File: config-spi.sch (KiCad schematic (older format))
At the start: 43 parts, among them J1 0878311420, J8 61300411121, Q7 BSS138APW, Q8 BSS138APW, U1 XC7K70T-FBG484, U3 S25FL128SAGNFI000

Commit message: Remove XADC circuit
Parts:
- removed C11: C_10n_0402, lpddr4-test-board-footprints:0402-cap, symbol lpddr4-test-board:C_10n_0402
- removed C9: C_1n_0402, lpddr4-test-board-footprints:0402-res, symbol lpddr4-test-board:C_1n_0402
- removed J8: 61300411121, lpddr4-test-board-footprints:PinHeader_1x4_P2.54mm_Drill1.02mm, symbol lpddr4-test-board:61300411121
- removed R18, R19: R_140R_0402, lpddr4-test-board-footprints:0402-res, symbol lpddr4-test-board:R_140R_0402
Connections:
- net labels removed: V_N, V_P, XADCGND, XADCVREF, XADC_V_N, XADC_V_P
- wire segments 158 -> 152
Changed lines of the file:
@@
 $EndDescr
 Wire Wire Line
-	11675 6100 10950 6100
-Text GLabel 10950 6100 0    50   Input ~ 0
-V_P
-Wire Wire Line
-	11675 6200 10950 6200
-Text GLabel 10950 6200 0    50   Input ~ 0
-V_N
+	11675 6100 11100 6100
+Wire Wire Line
+	11675 6200 11100 6200
 Wire Wire Line
 	11675 4700 10950 4700
@@
 Text GLabel 8375 9475 0    50   Input ~ 0
 MODE1
-Wire Wire Line
-	13475 8950 13800 8950
-Wire Wire Line
-	13475 9250 13825 9250
-Text GLabel 13475 8950 0    50   Input ~ 0
-XADC_V_P
-Text GLabel 13475 9250 0    50   Input ~ 0
-XADC_V_N
-Text GLabel 14925 8950 2    50   Input ~ 0
-V_P
-Text GLabel 14925 9250 2    50   Input ~ 0
-V_N
-$Comp
-L lpddr4-test-board:R_140R_0402 R18
-U 1 1 611C8786
-P 13950 8950
-F 0 "R18" H 13900 9050 60  0000 C CNN
-F 1 "R_140R_0402" H 13950 8800 60  0001 C CNN
-F 2 "lpddr4-test-board-footprints:0402-res" H 14150 9150 60  0001 L CNN
-F 3 "" H 13950 8950 50  0001 C CNN
-F 4 "MULTICOMP PRO" H 14150 9350 60  0001 L CNN "Manufacturer"
-F 5 "MCMR04X1400FTL" H 14150 9250 60  0001 L CNN "MPN"
-F 6 "140R" H 14150 8900 50  0000 C CNN "Val"
-	1    13950 8950
-	1    0    0    -1
-$EndComp
-$Comp
-L lpddr4-test-board:R_140R_0402 R19
-U 1 1 611C9205
-P 13975 9250
-F 0 "R19" H 13925 9350 60  0000 C CNN
-F 1 "R_140R_0402" H 13975 9100 60  0001 C CNN
-F 2 "lpddr4-test-board-footprints:0402-res" H 14175 9450 60  0001 L CNN
-F 3 "" H 13975 9250 50  0001 C CNN
-F 4 "MULTICOMP PRO" H 14175 9650 60  0001 L CNN "Manufacturer"
-F 5 "MCMR04X1400FTL" H 14175 9550 60  0001 L CNN "MPN"
-F 6 "140R" H 14175 9200 50  0000 C CNN "Val"
-	1    13975 9250
-	1    0    0    -1
-$EndComp
-$Comp
-L lpddr4-test-board:C_1n_0402 C9
-U 1 1 61217549
-P 14400 9100
-F 0 "C9" H 14425 9200 60  0000 L CNN
-F 1 "C_1n_0402" H 14400 8950 60  0001 C CNN
-F 2 "lpddr4-test-board-footprints:0402-res" H 14600 9300 60  0001 L CNN
-F 3 "" H 14400 9100 50  0001 C CNN
-F 4 "YAGEO" H 14600 9500 60  0001 L CNN "Manufacturer"
-F 5 "CC0402KRX7R9BB102" H 14600 9400 60  0001 L CNN "MPN"
-F 6 "1n" H 14425 9000 50  0000 L CNN "Val"
-	1    14400 9100
-	1    0    0    -1
-$EndComp
-Wire Wire Line
-	14100 8950 14400 8950
-Wire Wire Line
-	14125 9250 14400 9250
-Connection ~ 14400 8950
-Connection ~ 14400 9250
-Wire Wire Line
-	14400 8950 14925 8950
-Wire Wire Line
-	14400 9250 14925 9250
 Text Notes 1225 8500 0    118  ~ 24
 JTAG Connector\n
@@
 Text GLabel 8750 5600 0    50   Input ~ 0
 INIT_B
-Text GLabel 10950 6500 0    50   Input ~ 0
-XADCGND
-Wire Wire Line
-	11675 6500 10950 6500
-Text GLabel 10950 6400 0    50   Input ~ 0
-XADCVREF
-Wire Wire Line
-	11675 6400 10950 6400
-Wire Wire Line
-	11675 6700 11550 6700
-Wire Wire Line
-	11550 6700 11550 6800
-Wire Wire Line
-	11675 6800 11550 6800
-Connection ~ 11550 6800
-Wire Wire Line
-	11550 6800 11550 7025
+Wire Wire Line
+	11675 6500 11100 6500
+Wire Wire Line
+	11675 6700 11100 6700
+Wire Wire Line
+	11100 6700 11100 6800
+Wire Wire Line
+	11675 6800 11100 6800
+Connection ~ 11100 6800
+Wire Wire Line
+	11100 6800 11100 7000
 $Comp
 L lpddr4-test-board:GND #PWR0118
 U 1 1 61E5EC21
-P 11550 7025
-F 0 "#PWR0118" H 11550 6775 50  0001 C CNN
-F 1 "GND" H 11555 6852 50  0000 C CNN
-F 2 "" H 11550 7025 50  0001 C CNN
-F 3 "" H 11550 7025 50  0001 C CNN
-	1    11550 7025
-	1    0    0    -1
-$EndComp
-$Comp
-L lpddr4-test-board:C_10n_0402 C?
-U 1 1 61E688A4
-P 12575 9000
-AR Path="/600295C1/61E688A4" Ref="C?"  Part="1"
-AR Path="/5FD53C7D/61E688A4" Ref="C11"  Part="1"
-F 0 "C11" H 12600 9100 60  0000 L CNN
-F 1 "C_10n_0402" H 12575 8850 60  0001 C CNN
-F 2 "lpddr4-test-board-footprints:0402-cap" H 12775 9200 60  0001 L CNN
-F 3 "" H 12575 9000 50  0001 C CNN
-F 4 "AVX" H 12775 9400 60  0001 L CNN "Manufacturer"
-F 5 "04025G103ZAT2A" H 12775 9300 60  0001 L CNN "MPN"
-F 6 "10n" H 12600 8900 50  0000 L CNN "Val"
-	1    12575 9000
-	1    0    0    -1
-$EndComp
-Text GLabel 12575 9150 3    50   Input ~ 0
-XADCGND
+P 11100 7000
+F 0 "#PWR0118" H 11100 6750 50  0001 C CNN
+F 1 "GND" H 11105 6827 50  0000 C CNN
+F 2 "" H 11100 7000 50  0001 C CNN
+F 3 "" H 11100 7000 50  0001 C CNN
+	1    11100 7000
+	1    0    0    -1
+$EndComp
 Wire Wire Line
 	10150 5325 10150 5500
@@
 Wire Wire Line
 	10950 5000 11675 5000
-$Comp
-L lpddr4-test-board:61300411121 J8
-U 1 1 6AC614B6
-P 14350 7925
-F 0 "J8" V 14225 7900 50  0000 C CNN
-F 1 "61300411121" V 14775 7925 50  0000 C CNN
-F 2 "lpddr4-test-board-footprints:PinHeader_1x4_P2.54mm_Drill1.02mm" H 14550 8125 60  0001 L CNN
-F 3 "" H 14550 8225 60  0001 L CNN
-F 4 "61300411121" H 14550 8425 60  0001 L CNN "MPN"
-F 5 "Wurth Electronics Inc." H 14550 9025 60  0001 L CNN "Manufacturer"
-	1    14350 7925
-	0    1    1    0
-$EndComp
-Text GLabel 14875 7925 2    50   Input ~ 0
-XADC_V_P
-Text GLabel 14875 8025 2    50   Input ~ 0
-XADC_V_N
-Text GLabel 14875 8125 2    50   Input ~ 0
-XADCGND
-Text GLabel 14875 8225 2    50   Input ~ 0
-XADCVREF
-Wire Wire Line
-	14500 7925 14875 7925
-Wire Wire Line
-	14500 8025 14875 8025
-Wire Wire Line
-	14500 8125 14875 8125
-Wire Wire Line
-	14875 8225 14500 8225
 Text Notes 4550 8525 0    118  ~ 24
 STATUS LEDs
@@
 	0    -1   1    0
 $EndComp
-Text GLabel 12575 8850 1    50   Input ~ 0
-XADCVREF
 Text GLabel 9100 8975 2    50   Input ~ 0
 VCC3v3
@@
 	1    0    0    -1
 $EndComp
+Wire Wire Line
+	11100 6700 11100 6500
+Connection ~ 11100 6700
+Connection ~ 11100 6200
+Wire Wire Line
+	11100 6100 11100 6200
+Connection ~ 11100 6500
+Wire Wire Line
+	11100 6200 11100 6400
+Connection ~ 11100 6400
+Wire Wire Line
+	11100 6400 11100 6500
+Wire Wire Line
+	11100 6400 11675 6400
 $EndSCHEMATC

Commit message: Fix VCC labels
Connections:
- net labels removed: VCC3v3
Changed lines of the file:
@@
 	1    0    0    -1
 $EndComp
-Text GLabel 9800 4725 1    50   Input ~ 0
-VCC3v3
 $Comp
 L lpddr4-test-board:XC7K70T-FBG484 U1
@@
 Wire Wire Line
 	9475 4875 9800 4875
-Text GLabel 12075 3400 1    50   Input ~ 0
-VCC3v3
 Wire Wire Line
 	12075 3400 12075 3700
@@
 	12175 3700 12075 3700
 Connection ~ 12075 3700
-Text GLabel 14800 4300 1    50   Input ~ 0
-VCC3v3
 $Comp
 L lpddr4-test-board:C_47u_0603 C12
@@
 Wire Wire Line
 	5700 3525 5700 3250
-Text GLabel 5700 3150 1    50   Input ~ 0
-VCC3v3
 Wire Wire Line
 	5700 3825 5700 4550
@@
 	1625 9375 1625 9200
 Text GLabel 1625 9200 1    50   Input ~ 0
-VCC3v3
+VCC3V3
 Text GLabel 2575 9475 2    50   Input ~ 0
 TMS_JTAG
@@
 	8950 8975 9100 8975
 Text GLabel 9100 9475 2    50   Input ~ 0
-VCC3v3
+VCC3V3
 Wire Wire Line
 	8950 9475 9100 9475
@@
 	0    1    1    0
 $EndComp
-Text GLabel 11425 3400 1    50   Input ~ 0
-VCC3v3
 Wire Wire Line
 	11425 3400 11425 3775
@@
 	1    0    0    -1
 $EndComp
-Text GLabel 6175 5750 1    50   Input ~ 0
-VCC3v3
 Wire Wire Line
 	6175 5750 6175 5900
@@
 	0    -1   1    0
 $EndComp
-Text GLabel 9100 8975 2    50   Input ~ 0
-VCC3v3
 $Comp
 L antmicroRectangularConnectorsHeadersMalePins:62000311121 CFG1
@@
 	8550 10275 9125 10275
 Text GLabel 9125 9825 2    50   Input ~ 0
-VCC3v3
+VCC3V3
 $Comp
 L lpddr4-test-board:GND #PWR04
@@
 Wire Wire Line
 	11100 6400 11675 6400
+Text GLabel 9100 8975 2    50   Input ~ 0
+VCC3V3
+Text GLabel 12075 3400 1    50   Input ~ 0
+VCC3V3
+Text GLabel 11425 3400 1    50   Input ~ 0
+VCC3V3
+Text GLabel 14800 4300 1    50   Input ~ 0
+VCC3V3
+Text GLabel 9800 4725 1    50   Input ~ 0
+VCC3V3
+Text GLabel 6175 5750 1    50   Input ~ 0
+VCC3V3
+Text GLabel 5700 3150 1    50   Input ~ 0
+VCC3V3
 $EndSCHEMATC

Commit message: Replace VCC3V3 with 3V3_SYS
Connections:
- net labels added: 3V3_SYS
- net labels removed: VCC3V3
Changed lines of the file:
@@
 Connection ~ 14800 4750
 Text GLabel 2750 3950 1    50   Input ~ 0
-VCC3V3
+3V3_SYS
 Text GLabel 2425 3950 1    50   Input ~ 0
-VCC3V3
+3V3_SYS
 Wire Wire Line
 	2425 4250 2425 4300
@@
 	1625 9375 1625 9200
 Text GLabel 1625 9200 1    50   Input ~ 0
-VCC3V3
+3V3_SYS
 Text GLabel 2575 9475 2    50   Input ~ 0
 TMS_JTAG
@@
 	8950 8975 9100 8975
 Text GLabel 9100 9475 2    50   Input ~ 0
-VCC3V3
+3V3_SYS
 Wire Wire Line
 	8950 9475 9100 9475
@@
 	5325 9425 5350 9425
 Text GLabel 4925 9425 0    50   Input ~ 0
-VCC3V3
+3V3_SYS
 Wire Wire Line
 	4925 9425 5025 9425
@@
 	5350 10200 5375 10200
 Text GLabel 4950 10200 0    50   Input ~ 0
-VCC3V3
+3V3_SYS
 Wire Wire Line
 	4950 10200 5050 10200
@@
 	8550 10275 9125 10275
 Text GLabel 9125 9825 2    50   Input ~ 0
-VCC3V3
+3V3_SYS
 $Comp
 L lpddr4-test-board:GND #PWR04
@@
 	11100 6400 11675 6400
 Text GLabel 9100 8975 2    50   Input ~ 0
-VCC3V3
+3V3_SYS
 Text GLabel 12075 3400 1    50   Input ~ 0
-VCC3V3
+3V3_SYS
 Text GLabel 11425 3400 1    50   Input ~ 0
-VCC3V3
+3V3_SYS
 Text GLabel 14800 4300 1    50   Input ~ 0
-VCC3V3
+3V3_SYS
 Text GLabel 9800 4725 1    50   Input ~ 0
-VCC3V3
+3V3_SYS
 Text GLabel 6175 5750 1    50   Input ~ 0
-VCC3V3
+3V3_SYS
 Text GLabel 5700 3150 1    50   Input ~ 0
-VCC3V3
+3V3_SYS
 $EndSCHEMATC

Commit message: Update component library
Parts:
- CFG1: footprint antmicro-footprints:62000311121 -> lpddr4-test-board-footprints:62000311121; symbol antmicroRectangularConnectorsHeadersMalePins:62000311121 -> lpddr4-test-board:62000311121
- EMCCLK1, PUDC_B1: symbol antmicroTestPoints:test -> lpddr4-test-board:test
- J1: footprint antmicro-footprints:PinHeader_2x7_P2mm_Drill1mm -> lpddr4-test-board-footprints:PinHeader_2x7_P2mm_Drill1mm; symbol antmicroRectangularConnectorsHeadersMalePins:0878311420 -> lpddr4-test-board:0878311420
- Q7, Q8: footprint antmicro-footprints:SC70-3 -> lpddr4-test-board-footprints:SC70-3; symbol antmicroTransistorsFETsMOSFETsSingle:BSS138APW -> lpddr4-test-board:BSS138APW
- R11, R12, R13, R23, R24, R26, R27, R58, R59, R60, R9: footprint antmicro-footprints:0402-res -> lpddr4-test-board-footprints:0402-res; symbol antmicroResistors0402:R_0R_0402 -> lpddr4-test-board:R_0R_0402
- R14: footprint antmicro-footprints:0402-res -> lpddr4-test-board-footprints:0402-res; symbol antmicroResistors0402:R_2k2_0402 -> lpddr4-test-board:R_2k2_0402
- R57: footprint antmicro-footprints:0402-res -> lpddr4-test-board-footprints:0402-res; symbol antmicroResistors0402:R_330R_0402 -> lpddr4-test-board:R_330R_0402
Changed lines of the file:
@@
 $EndComp
 $Comp
-L antmicroResistors0402:R_330R_0402 R57
+L lpddr4-test-board:R_330R_0402 R57
 U 1 1 6107C15B
 P 10150 5175
 F 0 "R57" V 10105 5245 60  0000 L CNN
 F 1 "R_330R_0402" H 10150 5025 60  0001 C CNN
-F 2 "antmicro-footprints:0402-res" H 10350 5375 60  0001 L CNN
+F 2 "lpddr4-test-board-footprints:0402-res" H 10350 5375 60  0001 L CNN
 F 3 "" H 10150 5175 50  0001 C CNN
 F 4 "MULTICOMP" H 10350 5575 60  0001 L CNN "Manufacturer"
@@
 	6050 10500 5050 10500
 $Comp
-L antmicroTransistorsFETsMOSFETsSingle:BSS138APW Q?
+L lpddr4-test-board:BSS138APW Q?
 U 1 1 610AEC42
 P 5925 9425
@@
 F 0 "Q7" V 6192 9425 60  0000 C CNN
 F 1 "BSS138APW" V 6086 9425 60  0000 C CNN
-F 2 "antmicro-footprints:SC70-3" H 6125 9625 60  0001 L CNN
+F 2 "lpddr4-test-board-footprints:SC70-3" H 6125 9625 60  0001 L CNN
 F 3 "" H 6125 9725 60  0001 L CNN
 F 4 "BSS138PW" H 6125 9925 60  0001 L CNN "MPN"
@@
 $EndComp
 $Comp
-L antmicroTransistorsFETsMOSFETsSingle:BSS138APW Q?
+L lpddr4-test-board:BSS138APW Q?
 U 1 1 610AEC4A
 P 5950 10200
@@
 F 0 "Q8" V 6217 10200 60  0000 C CNN
 F 1 "BSS138APW" V 6111 10200 60  0000 C CNN
-F 2 "antmicro-footprints:SC70-3" H 6150 10400 60  0001 L CNN
+F 2 "lpddr4-test-board-footprints:SC70-3" H 6150 10400 60  0001 L CNN
 F 3 "" H 6150 10500 60  0001 L CNN
 F 4 "BSS138PW" H 6150 10700 60  0001 L CNN "MPN"
@@
 INIT_B
 $Comp
-L antmicroResistors0402:R_0R_0402 R58
+L lpddr4-test-board:R_0R_0402 R58
 U 1 1 611AD748
 P 11425 3925
 F 0 "R58" V 11380 3995 60  0000 L CNN
 F 1 "R_0R_0402" H 11425 3775 60  0001 C CNN
-F 2 "antmicro-footprints:0402-res" H 11625 4125 60  0001 L CNN
+F 2 "lpddr4-test-board-footprints:0402-res" H 11625 4125 60  0001 L CNN
 F 3 "" H 11425 3925 50  0001 C CNN
 F 4 "PANASONIC" H 11625 4325 60  0001 L CNN "Manufacturer"
@@
 	7475 6325 7975 6325
 $Comp
-L antmicroTestPoints:test PUDC_B1
+L lpddr4-test-board:test PUDC_B1
 U 1 1 61236E26
 P 5775 6375
@@
 $EndComp
 $Comp
-L antmicroTestPoints:test EMCCLK1
+L lpddr4-test-board:test EMCCLK1
 U 1 1 61237446
 P 7275 6375
@@
 	6175 6750 6175 6875
 $Comp
-L antmicroResistors0402:R_0R_0402 R26
+L lpddr4-test-board:R_0R_0402 R26
 U 1 1 6129A314
 P 4675 4450
 F 0 "R26" H 4475 4500 60  0000 C CNN
 F 1 "R_0R_0402" H 4675 4300 60  0001 C CNN
-F 2 "antmicro-footprints:0402-res" H 4875 4650 60  0001 L CNN
+F 2 "lpddr4-test-board-footprints:0402-res" H 4875 4650 60  0001 L CNN
 F 3 "" H 4675 4450 50  0001 C CNN
 F 4 "PANASONIC" H 4875 4850 60  0001 L CNN "Manufacturer"
@@
 $EndComp
 $Comp
-L antmicroResistors0402:R_0R_0402 R27
+L lpddr4-test-board:R_0R_0402 R27
 U 1 1 6129AB54
 P 4675 4550
 F 0 "R27" H 4475 4600 60  0000 C CNN
 F 1 "R_0R_0402" H 4675 4400 60  0001 C CNN
-F 2 "antmicro-footprints:0402-res" H 4875 4750 60  0001 L CNN
+F 2 "lpddr4-test-board-footprints:0402-res" H 4875 4750 60  0001 L CNN
 F 3 "" H 4675 4550 50  0001 C CNN
 F 4 "PANASONIC" H 4875 4950 60  0001 L CNN "Manufacturer"
@@
 $EndComp
 $Comp
-L antmicroResistors0402:R_0R_0402 R59
+L lpddr4-test-board:R_0R_0402 R59
 U 1 1 6129AE45
 P 4675 4750
 F 0 "R59" H 4450 4800 60  0000 C CNN
 F 1 "R_0R_0402" H 4675 4600 60  0001 C CNN
-F 2 "antmicro-footprints:0402-res" H 4875 4950 60  0001 L CNN
+F 2 "lpddr4-test-board-footprints:0402-res" H 4875 4950 60  0001 L CNN
 F 3 "" H 4675 4750 50  0001 C CNN
 F 4 "PANASONIC" H 4875 5150 60  0001 L CNN "Manufacturer"
@@
 $EndComp
 $Comp
-L antmicroResistors0402:R_0R_0402 R60
+L lpddr4-test-board:R_0R_0402 R60
 U 1 1 6129B28E
 P 4675 4850
 F 0 "R60" H 4450 4900 60  0000 C CNN
 F 1 "R_0R_0402" H 4675 4700 60  0001 C CNN
-F 2 "antmicro-footprints:0402-res" H 4875 5050 60  0001 L CNN
+F 2 "lpddr4-test-board-footprints:0402-res" H 4875 5050 60  0001 L CNN
 F 3 "" H 4675 4850 50  0001 C CNN
 F 4 "PANASONIC" H 4875 5250 60  0001 L CNN "Manufacturer"
@@
 $EndComp
 $Comp
-L antmicroResistors0402:R_0R_0402 R24
+L lpddr4-test-board:R_0R_0402 R24
 U 1 1 612AE761
 P 4675 4250
 F 0 "R24" H 4475 4300 60  0000 C CNN
 F 1 "R_0R_0402" H 4675 4100 60  0001 C CNN
-F 2 "antmicro-footprints:0402-res" H 4875 4450 60  0001 L CNN
+F 2 "lpddr4-test-board-footprints:0402-res" H 4875 4450 60  0001 L CNN
 F 3 "" H 4675 4250 50  0001 C CNN
 F 4 "PANASONIC" H 4875 4650 60  0001 L CNN "Manufacturer"
@@
 	4825 4250 5250 4250
 $Comp
-L antmicroResistors0402:R_0R_0402 R23
+L lpddr4-test-board:R_0R_0402 R23
 U 1 1 612F2218
 P 4675 4150
 F 0 "R23" H 4475 4200 60  0000 C CNN
 F 1 "R_0R_0402" H 4675 4000 60  0001 C CNN
-F 2 "antmicro-footprints:0402-res" H 4875 4350 60  0001 L CNN
+F 2 "lpddr4-test-board-footprints:0402-res" H 4875 4350 60  0001 L CNN
 F 3 "" H 4675 4150 50  0001 C CNN
 F 4 "PANASONIC" H 4875 4550 60  0001 L CNN "Manufacturer"
@@
 $EndComp
 $Comp
-L antmicroRectangularConnectorsHeadersMalePins:62000311121 CFG1
+L lpddr4-test-board:62000311121 CFG1
 U 1 1 6148AC57
 P 8700 10050
 F 0 "CFG1" H 8622 10055 50  0000 R CNN
 F 1 "62000311121" H 8750 9850 50  0001 C CNN
-F 2 "antmicro-footprints:62000311121" H 8800 10300 60  0001 L CNN
+F 2 "lpddr4-test-board-footprints:62000311121" H 8800 10300 60  0001 L CNN
 F 3 "https://www.we-online.com/catalog/datasheet/62000311121.pdf" H 8900 10350 60  0001 L CNN
 F 4 "62000421121" H 8900 10550 60  0001 L CNN "MPN"
@@
 $EndComp
 $Comp
-L antmicroResistors0402:R_0R_0402 R9
+L lpddr4-test-board:R_0R_0402 R9
 U 1 1 614A139A
 P 8800 8975
 F 0 "R9" H 8575 9025 60  0000 C CNN
 F 1 "R_0R_0402" H 8800 8825 60  0001 C CNN
-F 2 "antmicro-footprints:0402-res" H 9000 9175 60  0001 L CNN
+F 2 "lpddr4-test-board-footprints:0402-res" H 9000 9175 60  0001 L CNN
 F 3 "" H 8800 8975 50  0001 C CNN
 F 4 "PANASONIC" H 9000 9375 60  0001 L CNN "Manufacturer"
@@
 $EndComp
 $Comp
-L antmicroResistors0402:R_0R_0402 R11
+L lpddr4-test-board:R_0R_0402 R11
 U 1 1 614A1913
 P 8800 9175
 F 0 "R11" H 8575 9225 60  0000 C CNN
 F 1 "R_0R_0402" H 8800 9025 60  0001 C CNN
-F 2 "antmicro-footprints:0402-res" H 9000 9375 60  0001 L CNN
+F 2 "lpddr4-test-board-footprints:0402-res" H 9000 9375 60  0001 L CNN
 F 3 "" H 8800 9175 50  0001 C CNN
 F 4 "PANASONIC" H 9000 9575 60  0001 L CNN "Manufacturer"
@@
 $EndComp
 $Comp
-L antmicroResistors0402:R_0R_0402 R12
+L lpddr4-test-board:R_0R_0402 R12
 U 1 1 614A1D25
 P 8800 9475
 F 0 "R12" H 8575 9525 60  0000 C CNN
 F 1 "R_0R_0402" H 8800 9325 60  0001 C CNN
-F 2 "antmicro-footprints:0402-res" H 9000 9675 60  0001 L CNN
+F 2 "lpddr4-test-board-footprints:0402-res" H 9000 9675 60  0001 L CNN
 F 3 "" H 8800 9475 50  0001 C CNN
 F 4 "PANASONIC" H 9000 9875 60  0001 L CNN "Manufacturer"
@@
 $EndComp
 $Comp
-L antmicroResistors0402:R_0R_0402 R13
+L lpddr4-test-board:R_0R_0402 R13
 U 1 1 614A2237
 P 8800 9675
 F 0 "R13" H 8575 9725 60  0000 C CNN
 F 1 "R_0R_0402" H 8800 9525 60  0001 C CNN
-F 2 "antmicro-footprints:0402-res" H 9000 9875 60  0001 L CNN
+F 2 "lpddr4-test-board-footprints:0402-res" H 9000 9875 60  0001 L CNN
 F 3 "" H 8800 9675 50  0001 C CNN
 F 4 "PANASONIC" H 9000 10075 60  0001 L CNN "Manufacturer"
@@
 	4300 4250 4525 4250
 $Comp
-L antmicroResistors0402:R_2k2_0402 R14
+L lpddr4-test-board:R_2k2_0402 R14
 U 1 1 616A6781
 P 5050 3675
 F 0 "R14" H 5300 3750 60  0000 R CNN
 F 1 "R_2k2_0402" H 5050 3525 60  0001 C CNN
-F 2 "antmicro-footprints:0402-res" H 5250 3875 60  0001 L CNN
+F 2 "lpddr4-test-board-footprints:0402-res" H 5250 3875 60  0001 L CNN
 F 3 "" H 5050 3675 50  0001 C CNN
 F 4 "YAGEO" H 5250 4075 60  0001 L CNN "Manufacturer"
@@
 	5050 3250 5050 3525
 $Comp
-L antmicroRectangularConnectorsHeadersMalePins:0878311420 J1
+L lpddr4-test-board:0878311420 J1
 U 1 1 617E9509
 P 1250 9675
 F 0 "J1" H 1250 10200 50  0000 C CNN
 F 1 "0878311420" H 1250 10109 50  0000 C CNN
-F 2 "antmicro-footprints:PinHeader_2x7_P2mm_Drill1mm" H 1450 9875 60  0001 L CNN
+F 2 "lpddr4-test-board-footprints:PinHeader_2x7_P2mm_Drill1mm" H 1450 9875 60  0001 L CNN
 F 3 "https://www.molex.com/pdm_docs/sd/878311420_sd.pdf" H 1450 9975 60  0001 L CNN
 F 4 "0878311420" H 1450 10175 60  0001 L CNN "MPN"

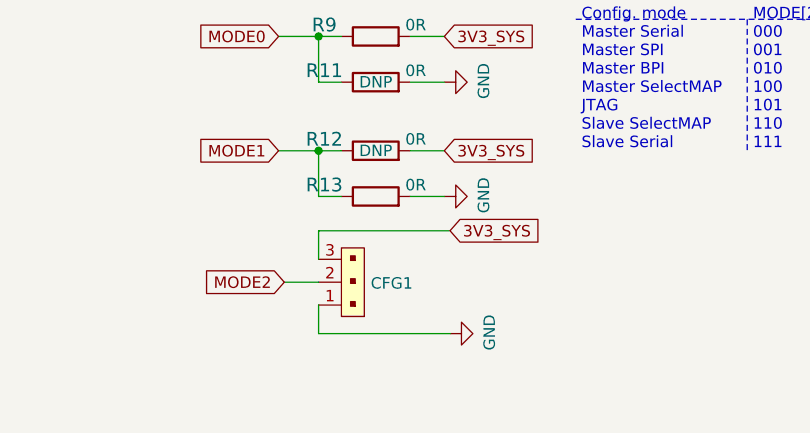
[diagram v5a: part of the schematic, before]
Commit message: Add OSHW logotype
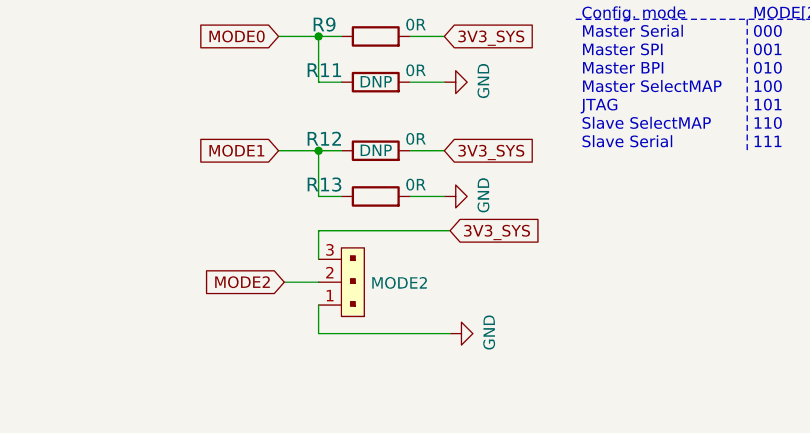
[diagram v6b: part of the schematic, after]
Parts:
- renumbered CFG1 to MODE2
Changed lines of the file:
@@
 $EndComp
 $Comp
-L lpddr4-test-board:62000311121 CFG1
+L lpddr4-test-board:62000311121 MODE2
 U 1 1 6148AC57
 P 8700 10050
-F 0 "CFG1" H 8622 10055 50  0000 R CNN
+F 0 "MODE2" H 8622 10055 50  0000 R CNN
 F 1 "62000311121" H 8750 9850 50  0001 C CNN
 F 2 "lpddr4-test-board-footprints:62000311121" H 8800 10300 60  0001 L CNN
